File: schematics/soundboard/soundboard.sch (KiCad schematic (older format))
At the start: 5 parts, among them J1 Battery, J2 Speaker, Q1 IRLZ44N, U1 DFPlayerMini, U2 STM8SF103

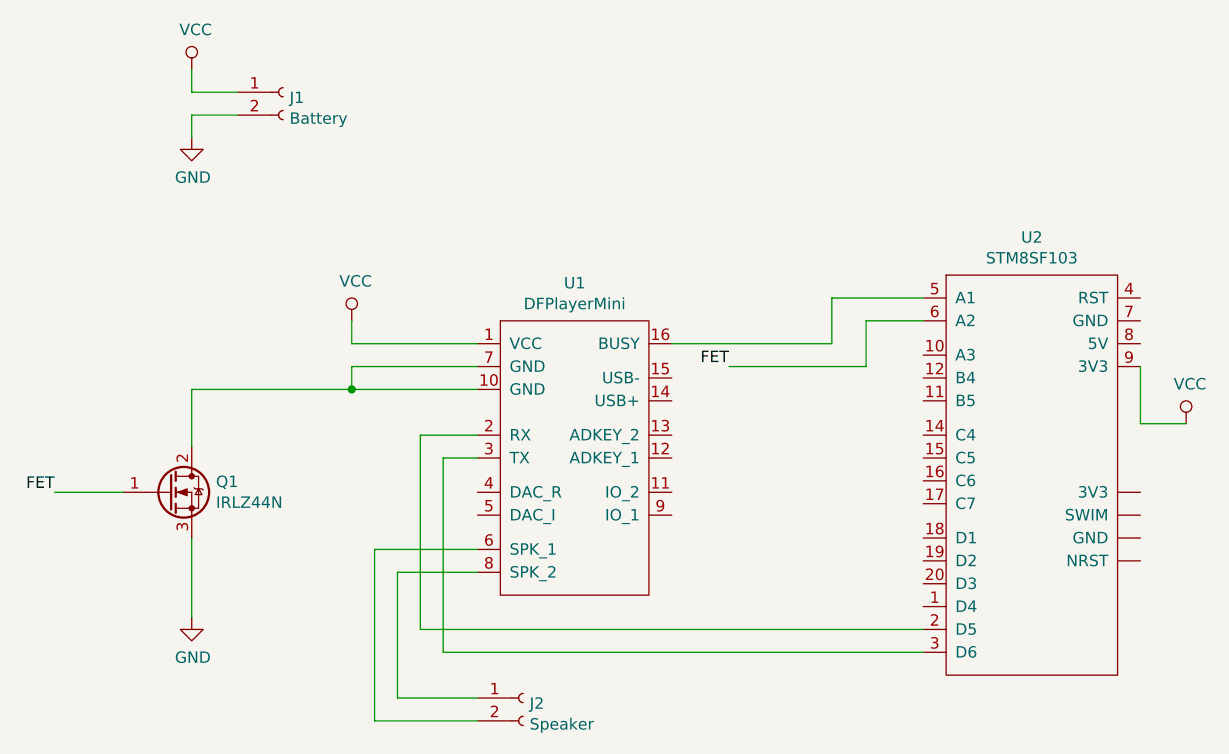
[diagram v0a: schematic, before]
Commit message: Update FET pin in schematic
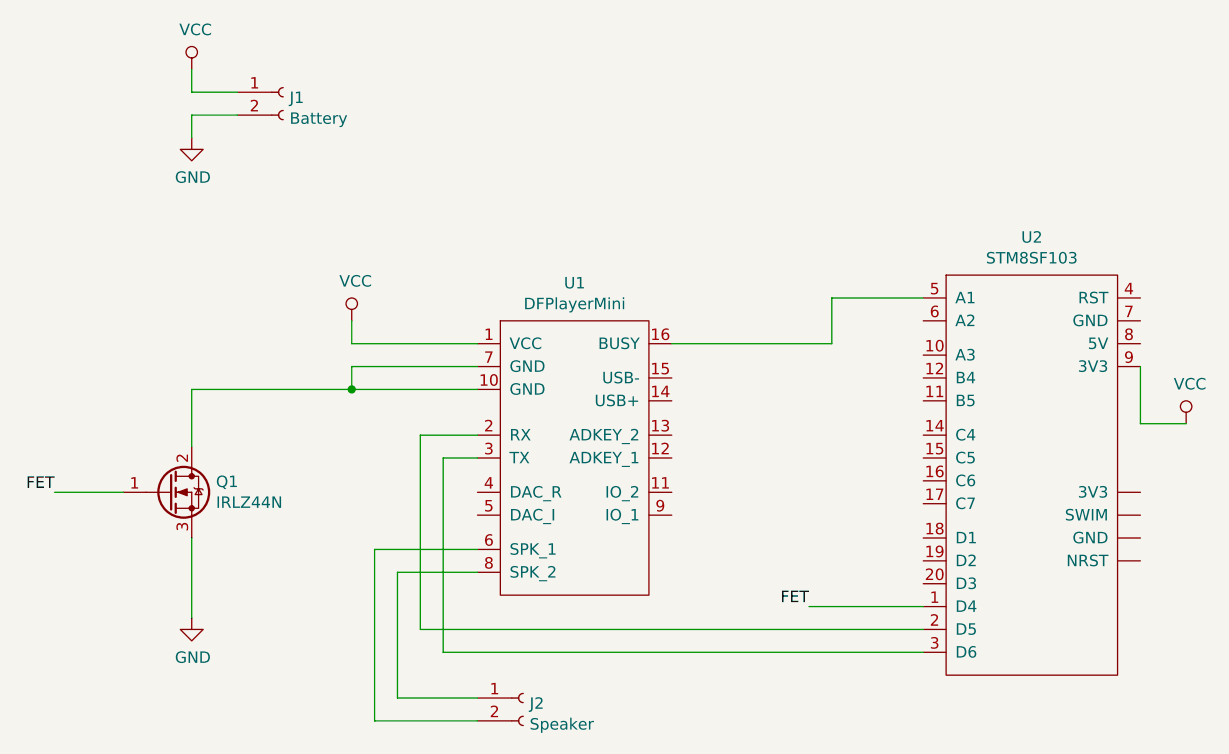
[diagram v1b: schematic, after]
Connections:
- net FET: now also U2.1 (D4); no longer U2.6 (A2)
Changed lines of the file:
@@
 Wire Wire Line
 	2950 4050 2950 4400
-Text Label 5300 3300 2    50   ~ 0
+Text Label 5650 4350 2    50   ~ 0
 FET
 Text Label 2350 3850 2    50   ~ 0
@@
 Wire Wire Line
 	2350 3850 2650 3850
-Wire Wire Line
-	5300 3300 5900 3300
 Wire Wire Line
 	4200 4100 3750 4100
@@
 	5750 3000 6150 3000
 Wire Wire Line
-	6150 3100 5900 3100
-Wire Wire Line
-	5900 3100 5900 3300
+	5650 4350 6150 4350
 $EndSCHEMATC
